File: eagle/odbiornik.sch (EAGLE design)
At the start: 28 parts, among them IC1 MEGA8-AI, IC2 75176AD, IC4 LD117ADT-TR, T1 BC847, T2 BC847, T3 BC847

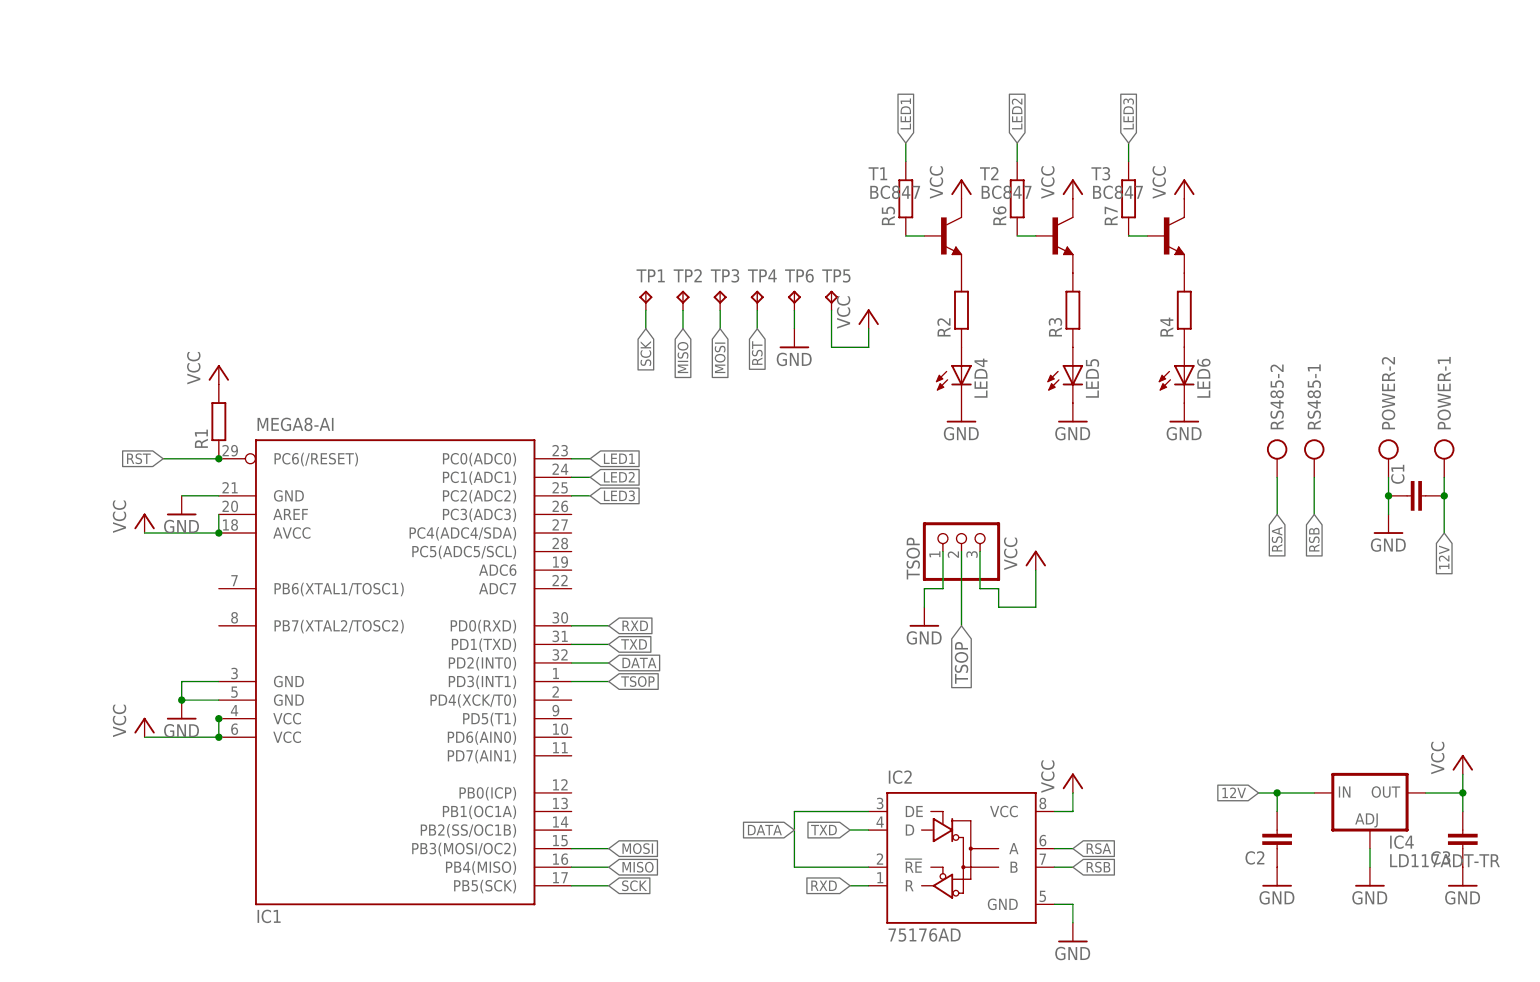
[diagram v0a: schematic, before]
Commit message: Zmiany: Odbiornik	+Polaryzacja 			+Terminator 			+Poprawki TSOP 			+ISP Socket 			+Power LED Dodano: RS485<->USB - v. poprawiona
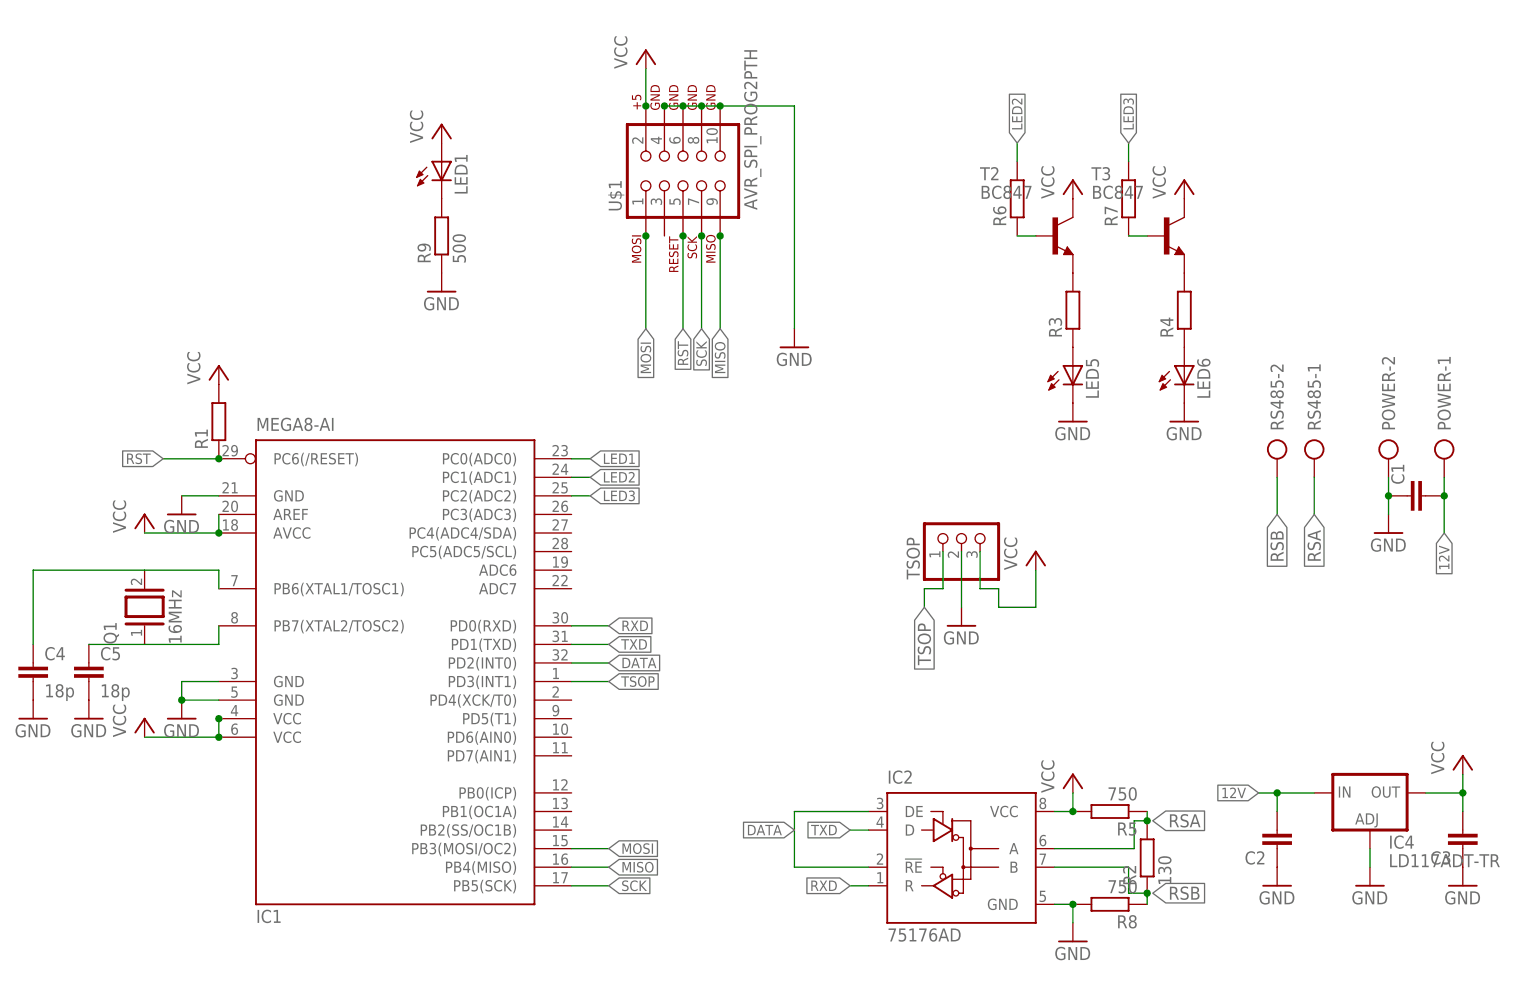
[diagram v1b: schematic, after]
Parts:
- removed LED4: (no value), led:LEDSFH480
- removed T1: BC847, transistor:BC847
- removed TP1, TP2, TP3, TP4, TP5, TP6: TPPAD1-13Y, testpad:TPPAD1-13Y
- added C4, C5: 18p, rcl:C-EUC0805
- added LED1: (no value), SparkFun-LED:LED1206
- added Q1: 16MHz, special:XTAL/S
- added R8: 750, rcl:R-EU_R0805
- added R9: 500, rcl:R-EU_R0805
- added U$1: AVR_SPI_PROG2PTH, SparkFun-Connectors:AVR_SPI_PROG2PTH
- R2: value (none) -> 130
- R5: value (none) -> 750
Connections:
- removed net N$2: LED4.A, R2.1
- removed net N$7: R5.1, T1.B
- new net N$10: C5.1, IC1.PB7(XTAL2/TOSC2), Q1.1
- new net N$11: C4.1, IC1.PB6(XTAL1/TOSC1), Q1.2
- net GND: now also C4.2, C5.2, R8.2, R9.1, TSOP.2, U$1.10, U$1.4, U$1.6, U$1.8; no longer LED4.C, TP6.TP, TSOP.1
- net LED1: no longer R5.2
- net MISO: now also U$1.9; no longer TP2.TP
- net MOSI: now also U$1.1; no longer TP3.TP
- net N$1: now also LED1.C, R9.2; no longer R2.2, T1.E
- net RSA: now also R2.2, R5.1, RS485-1.KL; no longer RS485-2.KL
- net RSB: now also R2.1, R8.1, RS485-2.KL; no longer RS485-1.KL
- net RST: now also U$1.5; no longer TP4.TP
- net SCK: now also U$1.7; no longer TP1.TP
- net TSOP: now also TSOP.1; no longer TSOP.2
- net VCC: now also LED1.A, R5.2, U$1.2; no longer T1.C, TP5.TP
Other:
- moved on the sheet: R2, R5

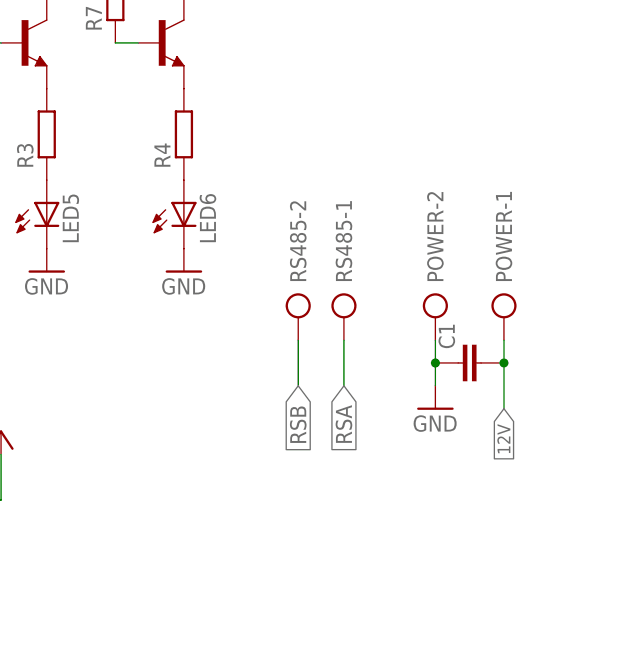
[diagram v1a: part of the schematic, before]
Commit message: New Receiver Board + Schematic + Gitignore prototype
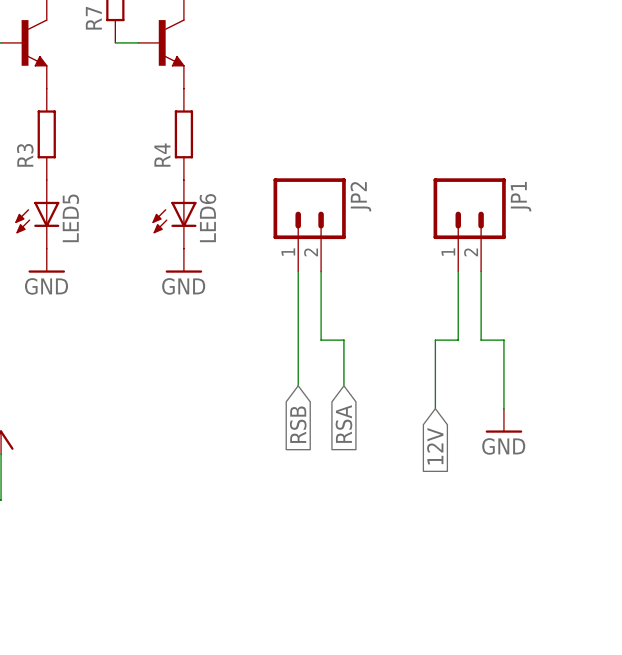
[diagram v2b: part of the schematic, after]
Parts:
- removed C1: (no value), rcl:C-EUC0805
- removed POWER, RS485: (no value), con-ptr500:AK300/2
- added JP1, JP2: (no value), SparkFun-Connectors:M02LOCK_LONGPADS
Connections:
- net 12V: now also JP1.1; no longer C1.2, POWER-1.KL
- net GND: now also JP1.2; no longer C1.1, POWER-2.KL
- net RSA: now also JP2.2; no longer RS485-1.KL
- net RSB: now also JP2.1; no longer RS485-2.KL
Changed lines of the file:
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@@
 <part name="R1" library="rcl" deviceset="R-EU_" device="R0805"/>
 <part name="P+3" library="supply1" deviceset="VCC" device=""/>
-<part name="RS485" library="con-ptr500" deviceset="AK300/2" device=""/>
-<part name="POWER" library="con-ptr500" deviceset="AK300/2" device=""/>
 <part name="P+5" library="supply1" deviceset="VCC" device=""/>
 <part name="GND4" library="supply1" deviceset="GND" device=""/>
 <part name="P+6" library="supply1" deviceset="VCC" device=""/>
 <part name="GND5" library="supply1" deviceset="GND" device=""/>
-<part name="C1" library="rcl" deviceset="C-EU" device="C0805"/>
-<part name="GND3" library="supply1" deviceset="GND" device=""/>
 <part name="GND6" library="supply1" deviceset="GND" device=""/>
 <part name="P+4" library="supply1" deviceset="VCC" device=""/>
@@
 <part name="GND10" library="supply1" deviceset="GND" device=""/>
 <part name="P+8" library="supply1" deviceset="VCC" device=""/>
+<part name="GND3" library="supply1" deviceset="GND" device=""/>
+<part name="JP1" library="SparkFun-Connectors" deviceset="M02" device="LOCK_LONGPADS"/>
+<part name="JP2" library="SparkFun-Connectors" deviceset="M02" device="LOCK_LONGPADS"/>
 </parts>
 <sheets>
@@
 <instance part="R1" gate="G$1" x="15.24" y="83.82" rot="R90"/>
 <instance part="P+3" gate="VCC" x="15.24" y="91.44"/>
-<instance part="RS485" gate="-1" x="165.1" y="81.28" rot="R270"/>
-<instance part="RS485" gate="-2" x="160.02" y="81.28" rot="R270"/>
-<instance part="POWER" gate="-1" x="182.88" y="81.28" rot="R270"/>
-<instance part="POWER" gate="-2" x="175.26" y="81.28" rot="R270"/>
 <instance part="P+5" gate="VCC" x="5.08" y="43.18"/>
 <instance part="GND4" gate="1" x="10.16" y="43.18"/>
 <instance part="P+6" gate="VCC" x="5.08" y="71.12"/>
 <instance part="GND5" gate="1" x="10.16" y="71.12"/>
-<instance part="C1" gate="G$1" x="177.8" y="73.66" rot="R90"/>
-<instance part="GND3" gate="1" x="175.26" y="68.58"/>
 <instance part="GND6" gate="1" x="172.72" y="20.32"/>
 <instance part="P+4" gate="VCC" x="185.42" y="38.1"/>
@@
 <instance part="GND10" gate="1" x="45.72" y="101.6"/>
 <instance part="P+8" gate="VCC" x="45.72" y="124.46"/>
+<instance part="GND3" gate="1" x="182.88" y="66.04"/>
+<instance part="JP1" gate="G$1" x="177.8" y="91.44" rot="R270"/>
+<instance part="JP2" gate="G$1" x="160.02" y="91.44" rot="R270"/>
 </instances>
 <busses>
@@
 <wire x1="15.24" y1="73.66" x2="10.16" y2="73.66" width="0.1524" layer="91"/>
 <pinref part="GND5" gate="1" pin="GND"/>
-</segment>
-<segment>
-<pinref part="POWER" gate="-2" pin="KL"/>
-<wire x1="175.26" y1="76.2" x2="175.26" y2="73.66" width="0.1524" layer="91"/>
-<pinref part="C1" gate="G$1" pin="1"/>
-<wire x1="175.26" y1="73.66" x2="175.26" y2="71.12" width="0.1524" layer="91"/>
-<junction x="175.26" y="73.66"/>
-<pinref part="GND3" gate="1" pin="GND"/>
 </segment>
 <segment>
@@
 <pinref part="GND10" gate="1" pin="GND"/>
 </segment>
+<segment>
+<pinref part="GND3" gate="1" pin="GND"/>
+<wire x1="182.88" y1="76.2" x2="182.88" y2="68.58" width="0.1524" layer="91"/>
+<pinref part="JP1" gate="G$1" pin="2"/>
+<wire x1="182.88" y1="76.2" x2="180.34" y2="76.2" width="0.1524" layer="91"/>
+<wire x1="180.34" y1="76.2" x2="180.34" y2="83.82" width="0.1524" layer="91"/>
+</segment>
 </net>
 <net name="VCC" class="0">
@@
 </segment>
 <segment>
-<pinref part="RS485" gate="-1" pin="KL"/>
 <wire x1="165.1" y1="76.2" x2="165.1" y2="71.12" width="0.1524" layer="91"/>
 <label x="165.1" y="71.12" size="1.778" layer="95" rot="R270" xref="yes"/>
+<pinref part="JP2" gate="G$1" pin="2"/>
+<wire x1="165.1" y1="76.2" x2="162.56" y2="76.2" width="0.1524" layer="91"/>
+<wire x1="162.56" y1="76.2" x2="162.56" y2="83.82" width="0.1524" layer="91"/>
 </segment>
 </net>
@@
 </segment>
 <segment>
-<pinref part="RS485" gate="-2" pin="KL"/>
-<wire x1="160.02" y1="76.2" x2="160.02" y2="71.12" width="0.1524" layer="91"/>
 <label x="160.02" y="71.12" size="1.778" layer="95" rot="R270" xref="yes"/>
+<pinref part="JP2" gate="G$1" pin="1"/>
+<wire x1="160.02" y1="71.12" x2="160.02" y2="83.82" width="0.1524" layer="91"/>
 </segment>
 </net>
@@
 </net>
 <net name="12V" class="0">
-<segment>
-<pinref part="POWER" gate="-1" pin="KL"/>
-<wire x1="182.88" y1="76.2" x2="182.88" y2="73.66" width="0.1524" layer="91"/>
-<pinref part="C1" gate="G$1" pin="2"/>
-<junction x="182.88" y="73.66"/>
-<wire x1="182.88" y1="73.66" x2="182.88" y2="68.58" width="0.1524" layer="91"/>
-<label x="182.88" y="68.58" size="1.4224" layer="95" rot="R270" xref="yes"/>
-</segment>
 <segment>
 <label x="157.48" y="33.02" size="1.4224" layer="95" rot="R180" xref="yes"/>
@@
 <wire x1="160.02" y1="33.02" x2="165.1" y2="33.02" width="0.1524" layer="91"/>
 </segment>
-</net>
+<segment>
+<label x="175.26" y="68.58" size="1.778" layer="95" rot="R270" xref="yes"/>
+<wire x1="175.26" y1="76.2" x2="175.26" y2="68.58" width="0.1524" layer="91"/>
+<pinref part="JP1" gate="G$1" pin="1"/>
+<wire x1="175.26" y1="76.2" x2="177.8" y2="76.2" width="0.1524" layer="91"/>
+<wire x1="177.8" y1="76.2" x2="177.8" y2="83.82" width="0.1524" layer="91"/>
+</segment>
+</net>
